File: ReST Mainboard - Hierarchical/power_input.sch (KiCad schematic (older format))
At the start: 11 parts, among them P1 CONN_01X02, P2 CONN_01X03, P3 CONN_01X02

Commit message: started routing
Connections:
- net 12VA-R: now also P3.2 (P2); no longer P3.1 (P1)
- net GND: now also P3.1 (P1); no longer P3.2 (P2)
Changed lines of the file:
@@
 F 3 "" H 6550 5450 50  0000 C CNN
 	1    6550 5450
-	-1   0    0    -1
+	-1   0    0    1
 $EndComp
 $Comp

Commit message: Mostly finished with main PCB. Only need to work the High Current Stuff out. On Vacation for now
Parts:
- P2: footprint Pin_Headers:Pin_Header_Straight_1x03 -> ReST-Library:bb02-hy03a
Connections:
- net VCC: now also P2.3 (P3); no longer P2.1 (P1)
- net VEE: now also P2.1 (P1); no longer P2.3 (P3)
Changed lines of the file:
@@
 F 0 "P2" H 5200 3850 50  0000 C CNN
 F 1 "CONN_01X03" V 5300 3650 50  0000 C CNN
-F 2 "Pin_Headers:Pin_Header_Straight_1x03" H 5200 3650 50  0001 C CNN
+F 2 "ReST-Library:bb02-hy03a" H 5200 3650 50  0001 C CNN
 F 3 "" H 5200 3650 50  0000 C CNN
 	1    5200 3650
-	0    -1   1    0
+	0    1    1    0
 $EndComp
 $Comp

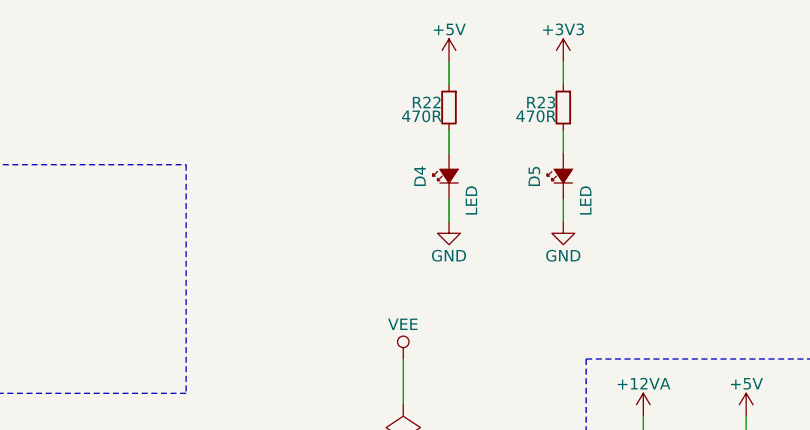
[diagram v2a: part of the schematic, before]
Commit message: minor changes to values of components and footprints. added two leds for both 12V Rails.
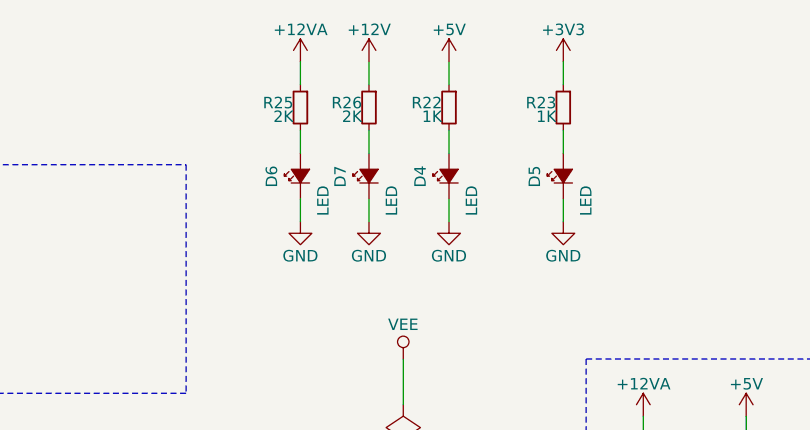
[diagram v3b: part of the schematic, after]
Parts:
- added D6, D7: LED, LEDs:LED_0805, symbol Led_Small
- added R25, R26: 2K, Resistors_SMD:R_0805_HandSoldering, symbol R_Small
- R22, R23: value 470R -> 1K; footprint Resistors_SMD:R_0603_HandSoldering -> Resistors_SMD:R_0805_HandSoldering
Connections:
- net +12V: now also R26.1
- net +12VA: now also R25.1
- net GND: now also D6.1 (K), D7.1 (K)
- new net: D7.2 (A), R26.2
- new net: D6.2 (A), R25.2
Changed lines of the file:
@@
 P 7600 2600
 F 0 "R22" H 7630 2620 50  0000 L CNN
-F 1 "470R" H 7630 2560 50  0000 L CNN
-F 2 "Resistors_SMD:R_0603_HandSoldering" H 7600 2600 50  0001 C CNN
+F 1 "1K" H 7630 2560 50  0000 L CNN
+F 2 "Resistors_SMD:R_0805_HandSoldering" H 7600 2600 50  0001 C CNN
 F 3 "" H 7600 2600 50  0000 C CNN
 	1    7600 2600
@@
 P 8100 2600
 F 0 "R23" H 8130 2620 50  0000 L CNN
-F 1 "470R" H 8130 2560 50  0000 L CNN
-F 2 "Resistors_SMD:R_0603_HandSoldering" H 8100 2600 50  0001 C CNN
+F 1 "1K" H 8130 2560 50  0000 L CNN
+F 2 "Resistors_SMD:R_0805_HandSoldering" H 8100 2600 50  0001 C CNN
 F 3 "" H 8100 2600 50  0000 C CNN
 	1    8100 2600
@@
 	-1   0    0    -1
 $EndComp
+$Comp
+L Led_Small D7
+U 1 1 5799386E
+P 7250 2900
+F 0 "D7" H 7200 3025 50  0000 L CNN
+F 1 "LED" H 7075 2800 50  0000 L CNN
+F 2 "LEDs:LED_0805" V 7250 2900 50  0001 C CNN
+F 3 "" V 7250 2900 50  0000 C CNN
+	1    7250 2900
+	0    -1   -1   0
+$EndComp
+$Comp
+L R_Small R26
+U 1 1 57993874
+P 7250 2600
+F 0 "R26" H 7280 2620 50  0000 L CNN
+F 1 "2K" H 7280 2560 50  0000 L CNN
+F 2 "Resistors_SMD:R_0805_HandSoldering" H 7250 2600 50  0001 C CNN
+F 3 "" H 7250 2600 50  0000 C CNN
+	1    7250 2600
+	-1   0    0    -1
+$EndComp
+Wire Wire Line
+	7250 2700 7250 2800
+Wire Wire Line
+	7250 2400 7250 2500
+Wire Wire Line
+	7250 3100 7250 3000
+$Comp
+L GND #PWR062
+U 1 1 5799387D
+P 7250 3100
+F 0 "#PWR062" H 7250 2850 50  0001 C CNN
+F 1 "GND" H 7250 2950 50  0000 C CNN
+F 2 "" H 7250 3100 50  0000 C CNN
+F 3 "" H 7250 3100 50  0000 C CNN
+	1    7250 3100
+	1    0    0    -1
+$EndComp
+$Comp
+L Led_Small D6
+U 1 1 57993947
+P 6950 2900
+F 0 "D6" H 6900 3025 50  0000 L CNN
+F 1 "LED" H 6775 2800 50  0000 L CNN
+F 2 "LEDs:LED_0805" V 6950 2900 50  0001 C CNN
+F 3 "" V 6950 2900 50  0000 C CNN
+	1    6950 2900
+	0    -1   -1   0
+$EndComp
+$Comp
+L R_Small R25
+U 1 1 5799394D
+P 6950 2600
+F 0 "R25" H 6980 2620 50  0000 L CNN
+F 1 "2K" H 6980 2560 50  0000 L CNN
+F 2 "Resistors_SMD:R_0805_HandSoldering" H 6950 2600 50  0001 C CNN
+F 3 "" H 6950 2600 50  0000 C CNN
+	1    6950 2600
+	-1   0    0    -1
+$EndComp
+Wire Wire Line
+	6950 2700 6950 2800
+Wire Wire Line
+	6950 2400 6950 2500
+Wire Wire Line
+	6950 3100 6950 3000
+$Comp
+L GND #PWR063
+U 1 1 57993956
+P 6950 3100
+F 0 "#PWR063" H 6950 2850 50  0001 C CNN
+F 1 "GND" H 6950 2950 50  0000 C CNN
+F 2 "" H 6950 3100 50  0000 C CNN
+F 3 "" H 6950 3100 50  0000 C CNN
+	1    6950 3100
+	1    0    0    -1
+$EndComp
+$Comp
+L +12V #PWR064
+U 1 1 57993B80
+P 7250 2400
+F 0 "#PWR064" H 7250 2250 50  0001 C CNN
+F 1 "+12V" H 7250 2540 50  0000 C CNN
+F 2 "" H 7250 2400 50  0000 C CNN
+F 3 "" H 7250 2400 50  0000 C CNN
+	1    7250 2400
+	1    0    0    -1
+$EndComp
+$Comp
+L +12VA #PWR065
+U 1 1 57993BB8
+P 6950 2400
+F 0 "#PWR065" H 6950 2250 50  0001 C CNN
+F 1 "+12VA" H 6950 2540 50  0000 C CNN
+F 2 "" H 6950 2400 50  0000 C CNN
+F 3 "" H 6950 2400 50  0000 C CNN
+	1    6950 2400
+	1    0    0    -1
+$EndComp
 $EndSCHEMATC

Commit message: final release. PCBs ordered
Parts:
- removed D6, D7: LED, LEDs:LED_0805, symbol Led_Small
- removed R25, R26: 2K, Resistors_SMD:R_0805_HandSoldering, symbol R_Small
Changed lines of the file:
@@
 	-1   0    0    -1
 $EndComp
-$Comp
-L Led_Small D7
-U 1 1 5799386E
-P 7250 2900
-F 0 "D7" H 7200 3025 50  0000 L CNN
-F 1 "LED" H 7075 2800 50  0000 L CNN
-F 2 "LEDs:LED_0805" V 7250 2900 50  0001 C CNN
-F 3 "" V 7250 2900 50  0000 C CNN
-	1    7250 2900
-	0    -1   -1   0
-$EndComp
-$Comp
-L R_Small R26
-U 1 1 57993874
-P 7250 2600
-F 0 "R26" H 7280 2620 50  0000 L CNN
-F 1 "2K" H 7280 2560 50  0000 L CNN
-F 2 "Resistors_SMD:R_0805_HandSoldering" H 7250 2600 50  0001 C CNN
-F 3 "" H 7250 2600 50  0000 C CNN
-	1    7250 2600
-	-1   0    0    -1
-$EndComp
-Wire Wire Line
-	7250 2700 7250 2800
-Wire Wire Line
-	7250 2400 7250 2500
-Wire Wire Line
-	7250 3100 7250 3000
-$Comp
-L GND #PWR062
-U 1 1 5799387D
-P 7250 3100
-F 0 "#PWR062" H 7250 2850 50  0001 C CNN
-F 1 "GND" H 7250 2950 50  0000 C CNN
-F 2 "" H 7250 3100 50  0000 C CNN
-F 3 "" H 7250 3100 50  0000 C CNN
-	1    7250 3100
-	1    0    0    -1
-$EndComp
-$Comp
-L Led_Small D6
-U 1 1 57993947
-P 6950 2900
-F 0 "D6" H 6900 3025 50  0000 L CNN
-F 1 "LED" H 6775 2800 50  0000 L CNN
-F 2 "LEDs:LED_0805" V 6950 2900 50  0001 C CNN
-F 3 "" V 6950 2900 50  0000 C CNN
-	1    6950 2900
-	0    -1   -1   0
-$EndComp
-$Comp
-L R_Small R25
-U 1 1 5799394D
-P 6950 2600
-F 0 "R25" H 6980 2620 50  0000 L CNN
-F 1 "2K" H 6980 2560 50  0000 L CNN
-F 2 "Resistors_SMD:R_0805_HandSoldering" H 6950 2600 50  0001 C CNN
-F 3 "" H 6950 2600 50  0000 C CNN
-	1    6950 2600
-	-1   0    0    -1
-$EndComp
-Wire Wire Line
-	6950 2700 6950 2800
-Wire Wire Line
-	6950 2400 6950 2500
-Wire Wire Line
-	6950 3100 6950 3000
-$Comp
-L GND #PWR063
-U 1 1 57993956
-P 6950 3100
-F 0 "#PWR063" H 6950 2850 50  0001 C CNN
-F 1 "GND" H 6950 2950 50  0000 C CNN
-F 2 "" H 6950 3100 50  0000 C CNN
-F 3 "" H 6950 3100 50  0000 C CNN
-	1    6950 3100
-	1    0    0    -1
-$EndComp
-$Comp
-L +12V #PWR064
-U 1 1 57993B80
-P 7250 2400
-F 0 "#PWR064" H 7250 2250 50  0001 C CNN
-F 1 "+12V" H 7250 2540 50  0000 C CNN
-F 2 "" H 7250 2400 50  0000 C CNN
-F 3 "" H 7250 2400 50  0000 C CNN
-	1    7250 2400
-	1    0    0    -1
-$EndComp
-$Comp
-L +12VA #PWR065
-U 1 1 57993BB8
-P 6950 2400
-F 0 "#PWR065" H 6950 2250 50  0001 C CNN
-F 1 "+12VA" H 6950 2540 50  0000 C CNN
-F 2 "" H 6950 2400 50  0000 C CNN
-F 3 "" H 6950 2400 50  0000 C CNN
-	1    6950 2400
-	1    0    0    -1
-$EndComp
 $EndSCHEMATC
